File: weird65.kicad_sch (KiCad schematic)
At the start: 78 parts, among them SW1 SW_Diode

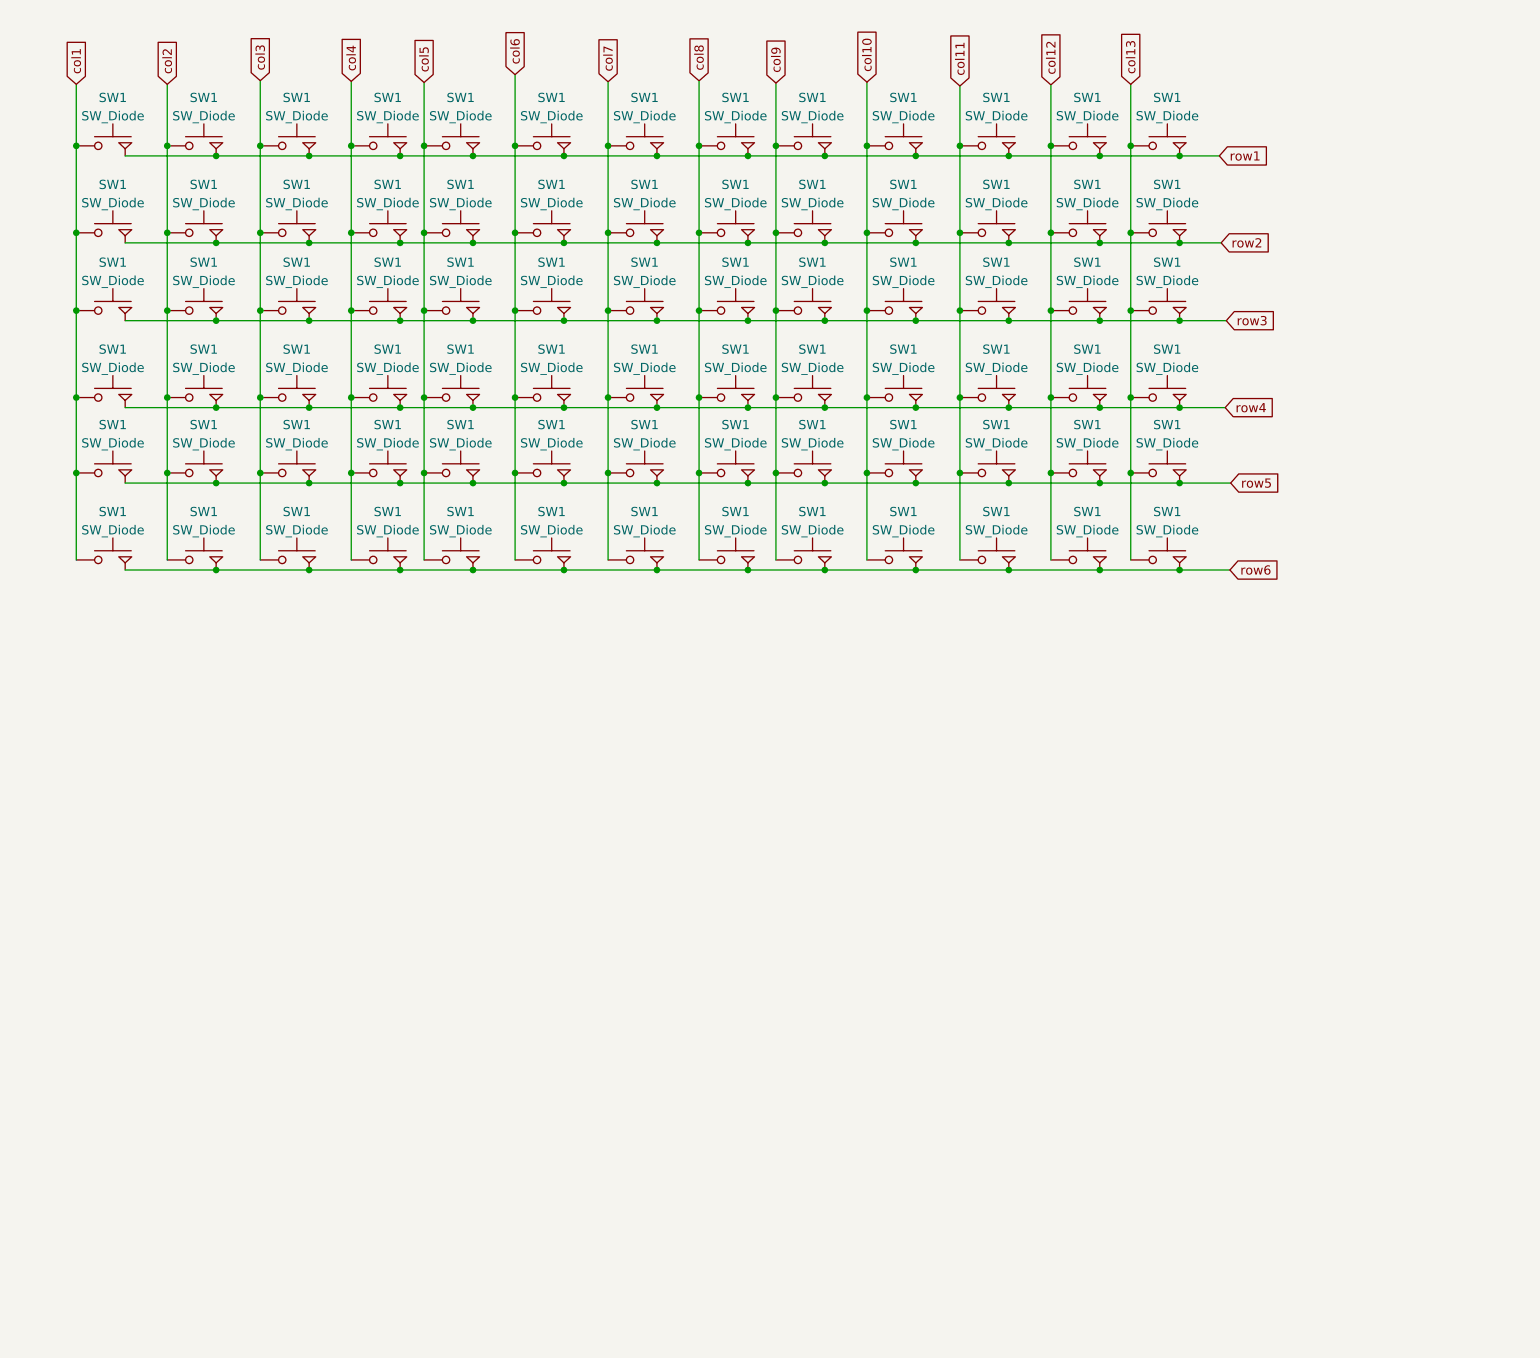
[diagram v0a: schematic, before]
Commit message: added xiao, Shift registers and wired it
DRC is giving a lot of errors due to the switches footprint. There are a few more errors
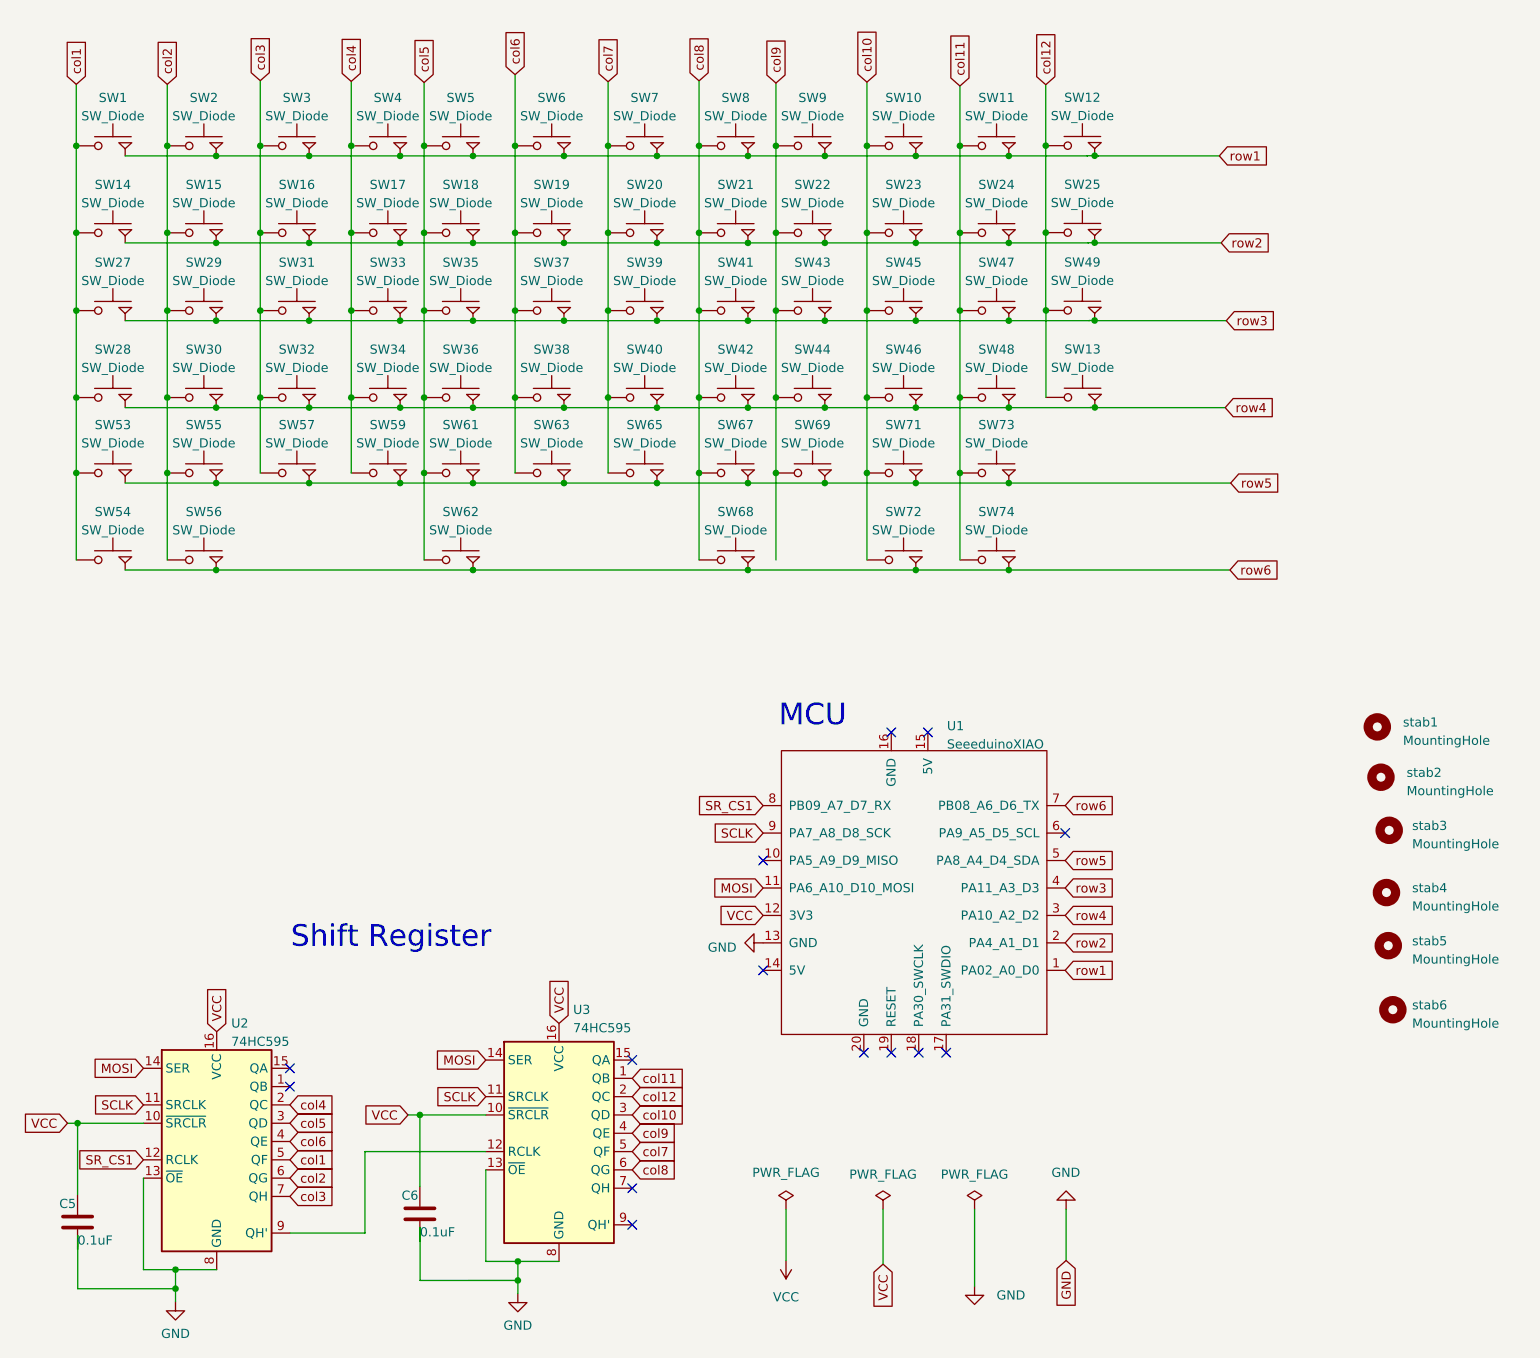
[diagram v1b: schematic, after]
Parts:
- removed SW1 (x13): SW_Diode, symbol keyboard_parts:SW_Diode
- added C5, C6: 0.1uF, Capacitor_SMD:C_0805_2012Metric, symbol Device:C
- added U1: SeeeduinoXIAO, Seeeduino XIAO KICAD:Seeeduino XIAO-MOUDLE14P-2.54-21X17.8MM, symbol Seeeduino XIAO:SeeeduinoXIAO
- added U2, U3: 74HC595, Package_SO:SOIC-16_3.9x9.9mm_P1.27mm, symbol 74xx:74HC595
- added stab1, stab2, stab3, stab4, stab5, stab6: MountingHole, customs:Stabilizer_Cherry_MX_2.00u, symbol Mechanical:MountingHole
- SW1: footprint (none) -> customs:MX_solder-hotswap_flippedPins
- SW10, SW11, SW12, SW13, SW14, SW15, SW16, SW17, SW18, SW19, SW2, SW20, SW21, SW22, SW23, SW24, SW25, SW27, SW28, SW29, SW3, SW30, SW31, SW32, SW33, SW34, SW35, SW36, SW37, SW38, SW39, SW4, SW40, SW41, SW42, SW43, SW44, SW45, SW46, SW47, SW48, SW49, SW5, SW53, SW54, SW55, SW56, SW57, SW59, SW6, SW61, SW62, SW63, SW65, SW67, SW68, SW69, SW71, SW72, SW73, SW74, SW8, SW9: renamed from SW1; footprint (none) -> customs:MX_solder-hotswap_flippedPins
- SW7: renamed from SW1; footprint (none) -> customs:MX_solder_flippedPins
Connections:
- net col13 is gone; now on net col12: SW13.1
- net col1: now also U2.5 (QF)
- net col10: now also U3.3 (QD)
- net col11: now also U3.1 (QB)
- net col12: now also U3.2 (QC)
- net col2: now also U2.6 (QG)
- net col3: now also U2.7 (QH)
- net col4: now also U2.2 (QC)
- net col5: now also U2.3 (QD)
- net col6: now also U2.4 (QE)
- net col7: now also U3.5 (QF)
- net col8: now also U3.6 (QG)
- net col9: now also U3.4 (QE)
- net row1: now also U1.1 (PA02_A0_D0); no longer SW13.2
- net row2: now also U1.2 (PA4_A1_D1)
- net row3: now also U1.4 (PA11_A3_D3)
- net row4: now also SW13.2, U1.3 (PA10_A2_D2)
- net row5: now also U1.5 (PA8_A4_D4_SDA)
- net row6: now also U1.7 (PB08_A6_D6_TX)
- new net: U2.9 (QH'), U3.12 (RCLK)
- new net GND: C5.2, C6.2, U1.13 (GND), U2.13 (~{OE}), U2.8 (GND), U3.13 (~{OE}), U3.8 (GND)
- new net MOSI: U1.11 (PA6_A10_D10_MOSI), U2.14 (SER), U3.14 (SER)
- new net SCLK: U1.9 (PA7_A8_D8_SCK), U2.11 (SRCLK), U3.11 (SRCLK)
- new net SR_CS1: U1.8 (PB09_A7_D7_RX), U2.12 (RCLK)
- new net VCC: C5.1, C6.1, U1.12 (3V3), U2.10 (~{SRCLR}), U2.16 (VCC), U3.10 (~{SRCLR}), U3.16 (VCC)
- no-connect marks 0 -> 14
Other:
- note added: "MCU"
- note added: "Shift Register"
- moved on the sheet: SW12, SW13, SW25, SW49
